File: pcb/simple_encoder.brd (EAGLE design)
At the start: 160 x 100 mm, 11 parts, among them X1 PEC11R

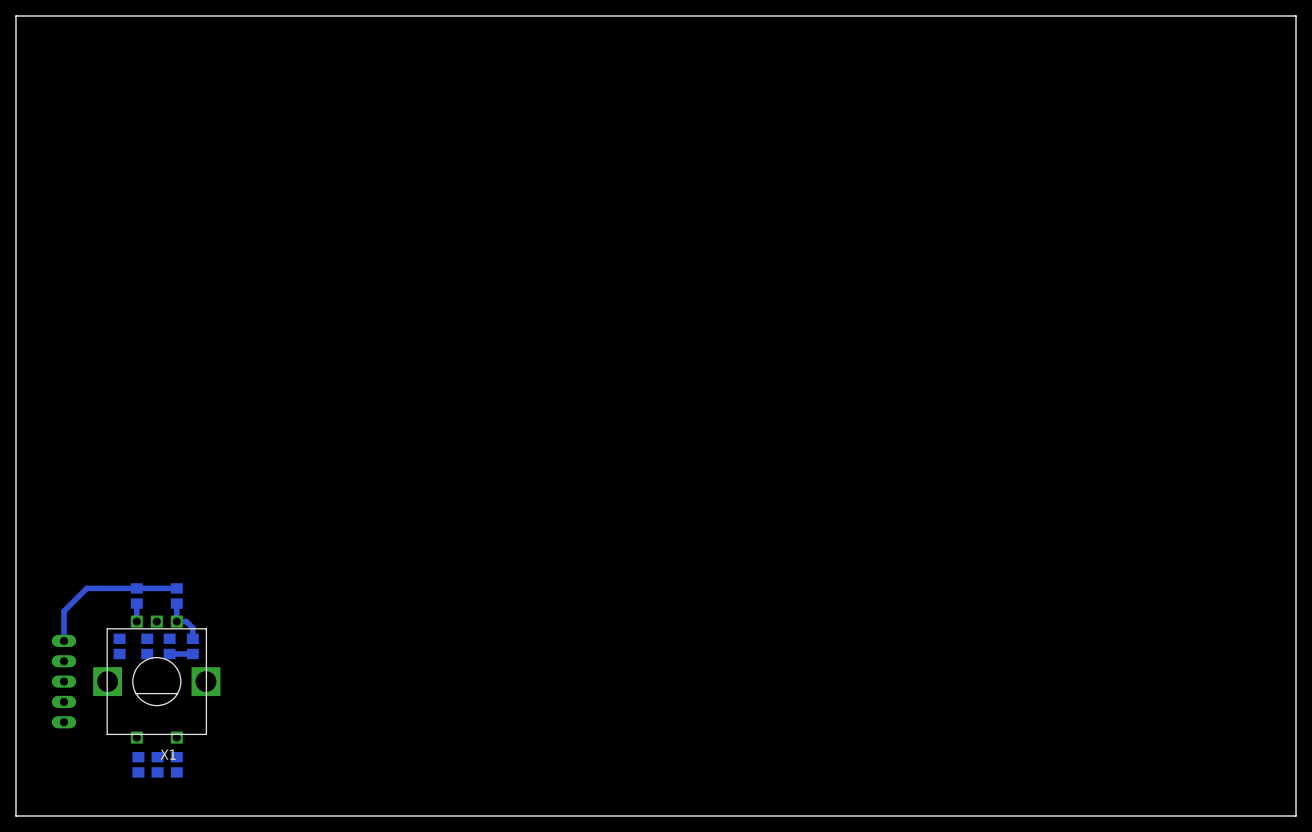
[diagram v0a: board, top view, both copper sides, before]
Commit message: updated simple controller, simple encoder (3D Packages)
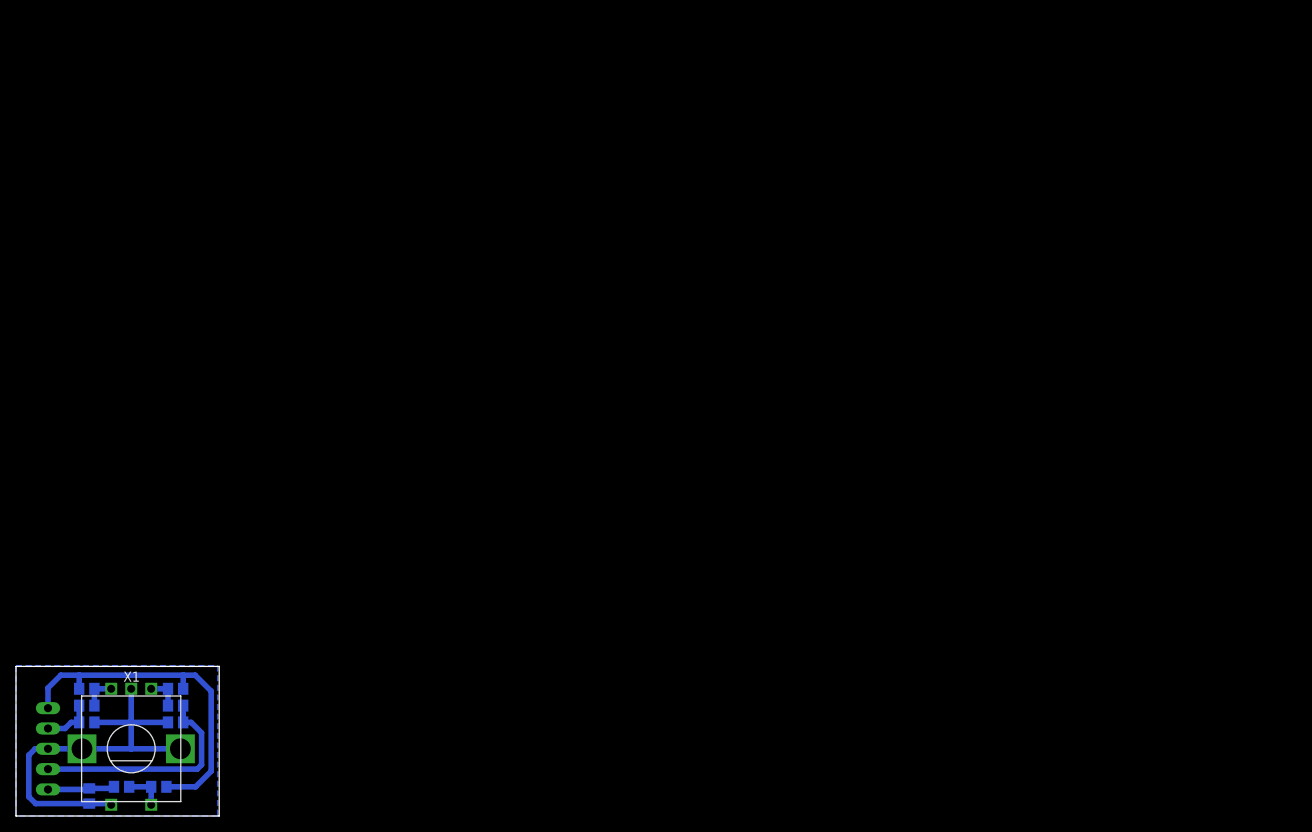
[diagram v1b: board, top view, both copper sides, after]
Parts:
- moved R3 13.2 mm to (8.85, 15.9), turned to 0 degrees
- moved C2 12.1 mm to (8.85, 11.7), turned to 180 degrees
- moved R2 11.6 mm to (19.9, 15.9), turned to 180 degrees
- moved C1 9.53 mm to (19.9, 11.7), turned to 0 degrees
- moved X1 8.99 mm to (14.4, 8.40)
- moved JP1 8.63 mm to (4.00, 8.40)
- moved R4 8.46 mm to (8.85, 13.8), turned to 0 degrees
- moved R1 7.71 mm to (19.9, 13.8), turned to 0 degrees
- moved C3 7.28 mm to (9.15, 2.50), turned to 270 degrees
- moved R6 5.27 mm to (13.2, 3.65), turned to 0 degrees
- moved R5 3.55 mm to (17.9, 3.65), turned to 180 degrees
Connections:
- net A: now also JP1.4; no longer JP1.3
- net B: now also JP1.2; no longer JP1.4
- net GND: now also JP1.3; no longer JP1.2
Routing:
- net GND: track 0.00 -> 52.0 mm
- net A: track 2.90 -> 28.4 mm
- net +5V: track 19.0 -> 44.2 mm
- net BUTTON: track 0.00 -> 8.58 mm
- net B: track 0.00 -> 6.31 mm
- net BUTTON_UNFIL: track 0.00 -> 5.00 mm
- net B_UNFIL: track 2.25 -> 4.20 mm
- net A_UNFIL: track 5.93 -> 4.20 mm
- added copper zone on layer 16, net GND
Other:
- board size 160 x 100 mm -> 25.4 x 18.7 mm
